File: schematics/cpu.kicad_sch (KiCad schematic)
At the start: 3 parts, among them U3 W65C02SxP

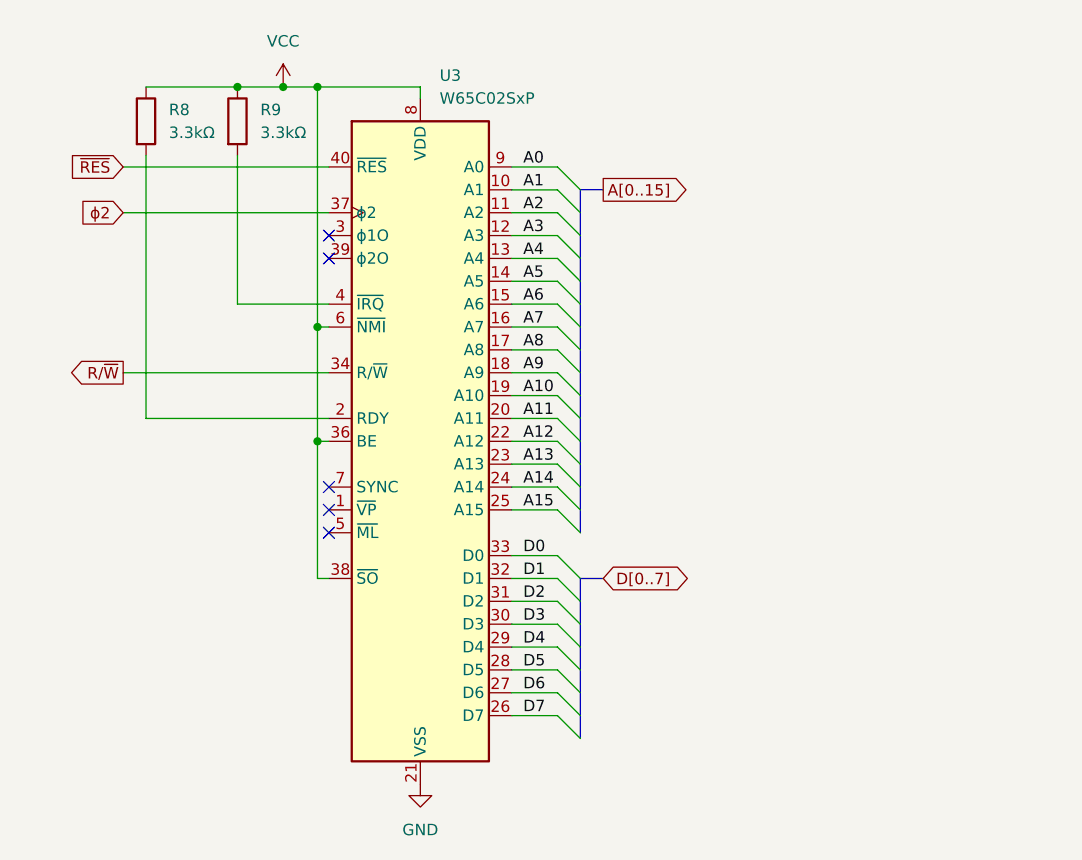
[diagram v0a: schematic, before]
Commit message: Address decoder pld file and no-VIA keyboard schematic and pld file.
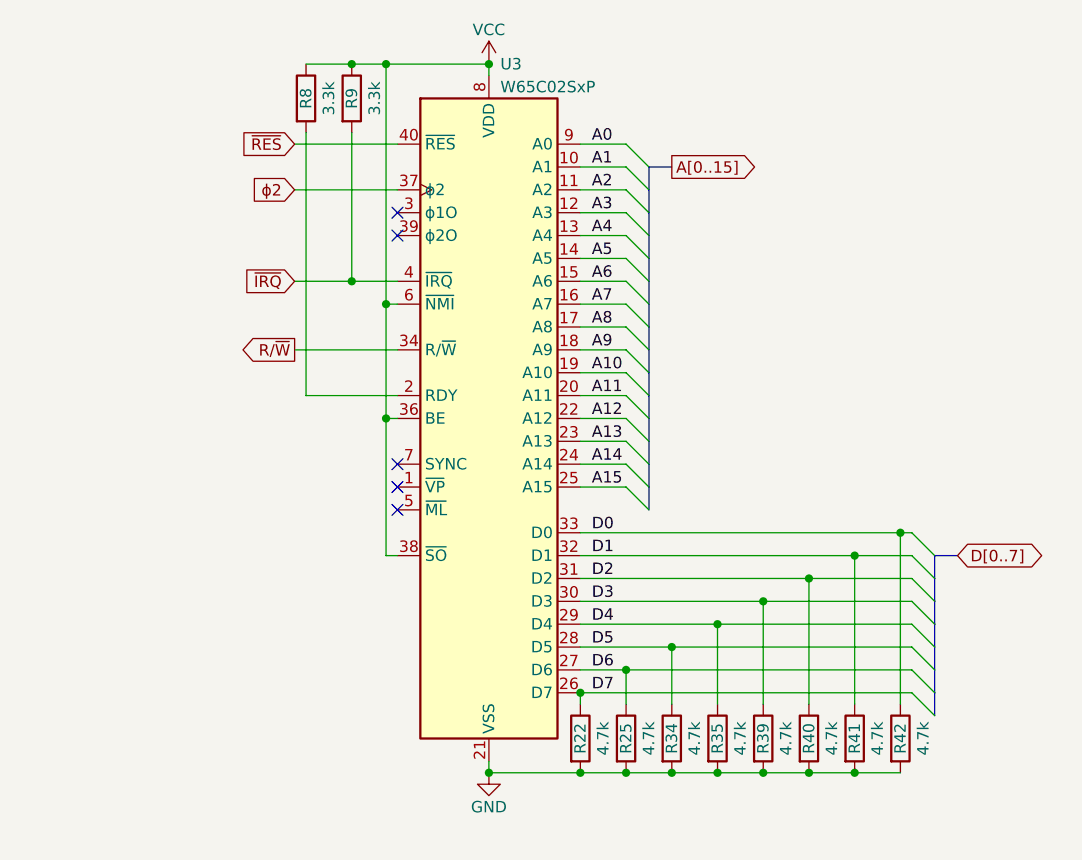
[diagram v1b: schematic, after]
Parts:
- added R22, R25, R34, R35, R39, R40, R41, R42: 4.7k, symbol Device:R
- R8, R9: value 3.3kΩ -> 3.3k
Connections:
- net D0: now also R42.1
- net D1: now also R41.1
- net D2: now also R40.1
- net D3: now also R39.1
- net D4: now also R35.1
- net D5: now also R34.1
- net D6: now also R25.1
- net D7: now also R22.1
- net GND: now also R22.2, R25.2, R34.2, R35.2, R39.2, R40.2, R41.2, R42.2
- net ~{IRQ}: now reaches R9.2, U3.4 (~{IRQ})
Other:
- moved on the sheet: R8, R9, U3

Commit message: PLD files and schematics for address decoder, device selector, keyboard controller, lcd controller, banked memory, and bootloader.
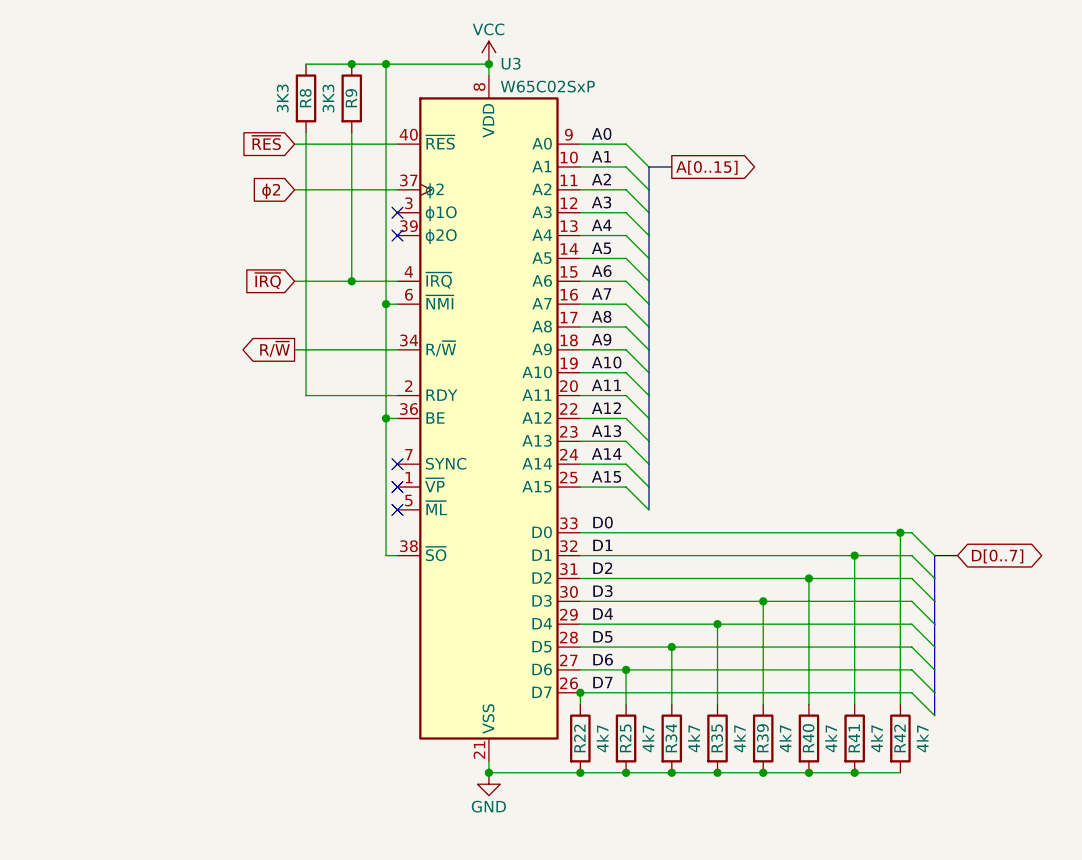
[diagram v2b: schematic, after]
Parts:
- R22, R25, R34, R35, R39, R40, R41, R42: value 4.7k -> 4k7
- R8, R9: value 3.3k -> 3K3
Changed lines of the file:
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@@
 			)
 		)
-		(property "Value" "4.7k"
+		(property "Value" "4k7"
 			(at 177.8 134.62 90)
 			(show_name no)
@@
 			)
 		)
-		(property "Value" "4.7k"
+		(property "Value" "4k7"
 			(at 172.72 134.62 90)
 			(show_name no)
@@
 			)
 		)
-		(property "Value" "4.7k"
+		(property "Value" "4k7"
 			(at 162.56 134.62 90)
 			(show_name no)
@@
 			)
 		)
-		(property "Value" "3.3k"
-			(at 121.92 63.5 90)
+		(property "Value" "3K3"
+			(at 116.84 63.5 90)
 			(show_name no)
 			(do_not_autoplace no)
@@
 			)
 		)
-		(property "Value" "4.7k"
+		(property "Value" "4k7"
 			(at 147.32 134.62 90)
 			(show_name no)
@@
 			)
 		)
-		(property "Value" "3.3k"
-			(at 116.84 63.5 90)
+		(property "Value" "3K3"
+			(at 111.76 63.5 90)
 			(show_name no)
 			(do_not_autoplace no)
@@
 			)
 		)
-		(property "Value" "4.7k"
+		(property "Value" "4k7"
 			(at 152.4 134.62 90)
 			(show_name no)
@@
 			)
 		)
-		(property "Value" "4.7k"
+		(property "Value" "4k7"
 			(at 182.88 134.62 90)
 			(show_name no)
@@
 			)
 		)
-		(property "Value" "4.7k"
+		(property "Value" "4k7"
 			(at 167.64 134.62 90)
 			(show_name no)
@@
 			)
 		)
-		(property "Value" "4.7k"
+		(property "Value" "4k7"
 			(at 157.48 134.62 90)
 			(show_name no)

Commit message: reduced RDY pullup to 1K for speed (still might not be enough)
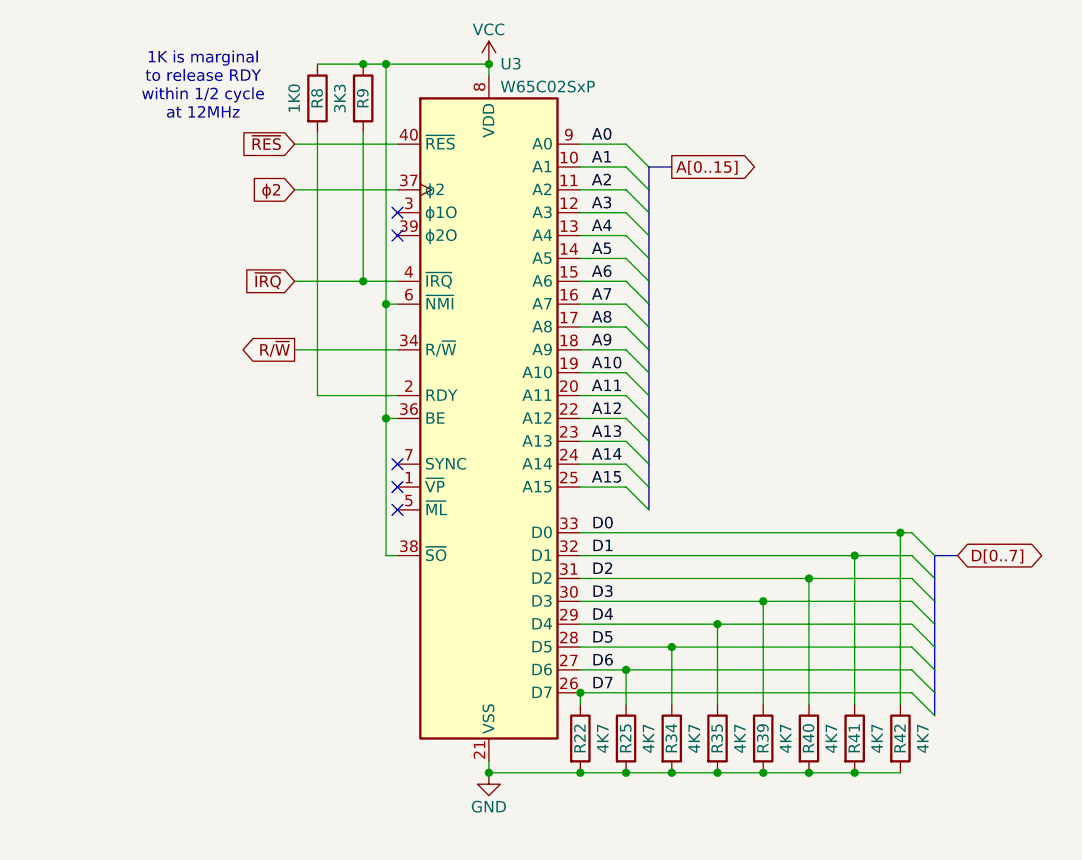
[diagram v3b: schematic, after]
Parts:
- R22, R25, R34, R35, R39, R40, R41, R42: value 4k7 -> 4K7
- R8: value 3K3 -> 1K0
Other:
- note added: "1K is marginal to release RDY within 1/2 cycle at 12MHz"
- moved on the sheet: R8, R9
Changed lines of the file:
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@@
 		(rev "1")
+	)
+	(text "1K is marginal\nto release RDY\nwithin 1/2 cycle\nat 12MHz"
+		(exclude_from_sim no)
+		(at 102.87 62.23 0)
+		(effects
+			(font
+				(size 1.27 1.27)
+			)
+		)
 	)
 	(junction
@@
 	)
 	(junction
+		(at 120.65 59.69)
+		(diameter 0)
+		(color 0 0 0 0)
+	)
+	(junction
 		(at 149.86 127)
 		(diameter 0)
@@
 	)
 	(junction
-		(at 119.38 59.69)
-		(diameter 0)
-		(color 0 0 0 0)
-	)
-	(junction
 		(at 144.78 129.54)
-		(diameter 0)
-		(color 0 0 0 0)
-	)
-	(junction
-		(at 119.38 83.82)
 		(diameter 0)
 		(color 0 0 0 0)
@@
 		(color 0 0 0 0)
 	)
+	(junction
+		(at 120.65 83.82)
+		(diameter 0)
+		(color 0 0 0 0)
+	)
 	(no_connect
 		(at 124.46 76.2)
@@
 	(wire
 		(pts
-			(xy 119.38 67.31) (xy 119.38 83.82)
+			(xy 120.65 67.31) (xy 120.65 83.82)
 		)
 		(stroke
@@
 	(wire
 		(pts
-			(xy 124.46 96.52) (xy 114.3 96.52)
+			(xy 124.46 96.52) (xy 115.57 96.52)
 		)
 		(stroke
@@
 		)
 	)
+	(wire
+		(pts
+			(xy 120.65 83.82) (xy 124.46 83.82)
+		)
+		(stroke
+			(width 0)
+			(type default)
+		)
+	)
 	(bus
 		(pts
@@
 	(wire
 		(pts
-			(xy 113.03 83.82) (xy 119.38 83.82)
+			(xy 113.03 83.82) (xy 120.65 83.82)
 		)
 		(stroke
@@
 	(wire
 		(pts
-			(xy 114.3 67.31) (xy 114.3 96.52)
+			(xy 115.57 67.31) (xy 115.57 96.52)
 		)
 		(stroke
@@
 	(wire
 		(pts
-			(xy 119.38 83.82) (xy 124.46 83.82)
-		)
-		(stroke
-			(width 0)
-			(type default)
-		)
-	)
-	(wire
-		(pts
 			(xy 165.1 138.43) (xy 170.18 138.43)
 		)
@@
 	(wire
 		(pts
+			(xy 120.65 59.69) (xy 134.62 59.69)
+		)
+		(stroke
+			(width 0)
+			(type default)
+		)
+	)
+	(wire
+		(pts
 			(xy 144.78 119.38) (xy 165.1 119.38)
 		)
@@
 	(wire
 		(pts
-			(xy 119.38 59.69) (xy 134.62 59.69)
-		)
-		(stroke
-			(width 0)
-			(type default)
-		)
-	)
-	(wire
-		(pts
 			(xy 160.02 138.43) (xy 165.1 138.43)
 		)
@@
 	(wire
 		(pts
-			(xy 114.3 59.69) (xy 119.38 59.69)
+			(xy 115.57 59.69) (xy 120.65 59.69)
 		)
 		(stroke
@@
 			)
 		)
-		(property "Value" "4k7"
+		(property "Value" "4K7"
 			(at 177.8 134.62 90)
 			(show_name no)
@@
 			)
 		)
-		(property "Value" "4k7"
+		(property "Value" "4K7"
 			(at 172.72 134.62 90)
 			(show_name no)
@@
 			)
 		)
-		(property "Value" "4k7"
+		(property "Value" "4K7"
 			(at 162.56 134.62 90)
 			(show_name no)
@@
 	(symbol
 		(lib_id "Device:R")
-		(at 119.38 63.5 0)
+		(at 120.65 63.5 0)
 		(unit 1)
 		(body_style 1)
@@
 		(dnp no)
 		(property "Reference" "R9"
-			(at 119.38 63.5 90)
+			(at 120.65 63.5 90)
 			(show_name no)
 			(do_not_autoplace no)
@@
 		)
 		(property "Value" "3K3"
-			(at 116.84 63.5 90)
+			(at 118.11 63.5 90)
 			(show_name no)
 			(do_not_autoplace no)
@@
 		)
 		(property "Footprint" ""
-			(at 117.602 63.5 90)
+			(at 118.872 63.5 90)
 			(hide yes)
 			(show_name no)
@@
 		)
 		(property "Datasheet" ""
-			(at 119.38 63.5 0)
+			(at 120.65 63.5 0)
 			(hide yes)
 			(show_name no)
@@
 		)
 		(property "Description" "Resistor"
-			(at 119.38 63.5 0)
+			(at 120.65 63.5 0)
 			(hide yes)
 			(show_name no)
@@
 			)
 		)
-		(property "Value" "4k7"
+		(property "Value" "4K7"
 			(at 147.32 134.62 90)
 			(show_name no)
@@
 	(symbol
 		(lib_id "Device:R")
-		(at 114.3 63.5 0)
+		(at 115.57 63.5 0)
 		(unit 1)
 		(body_style 1)
@@
 		(dnp no)
 		(property "Reference" "R8"
-			(at 114.3 63.5 90)
-			(show_name no)
-			(do_not_autoplace no)
-			(effects
-				(font
-					(size 1.27 1.27)
-				)
-			)
-		)
-		(property "Value" "3K3"
-			(at 111.76 63.5 90)
+			(at 115.57 63.5 90)
+			(show_name no)
+			(do_not_autoplace no)
+			(effects
+				(font
+					(size 1.27 1.27)
+				)
+			)
+		)
+		(property "Value" "1K0"
+			(at 113.03 63.5 90)
 			(show_name no)
 			(do_not_autoplace no)
@@
 		)
 		(property "Footprint" ""
-			(at 112.522 63.5 90)
+			(at 113.792 63.5 90)
 			(hide yes)
 			(show_name no)
@@
 		)
 		(property "Datasheet" ""
-			(at 114.3 63.5 0)
+			(at 115.57 63.5 0)
 			(hide yes)
 			(show_name no)
@@
 		)
 		(property "Description" "Resistor"
-			(at 114.3 63.5 0)
+			(at 115.57 63.5 0)
 			(hide yes)
 			(show_name no)
@@
 			)
 		)
-		(property "Value" "4k7"
+		(property "Value" "4K7"
 			(at 152.4 134.62 90)
 			(show_name no)
@@
 			)
 		)
-		(property "Value" "4k7"
+		(property "Value" "4K7"
 			(at 182.88 134.62 90)
 			(show_name no)
@@
 			)
 		)
-		(property "Value" "4k7"
+		(property "Value" "4K7"
 			(at 167.64 134.62 90)
 			(show_name no)
@@
 			)
 		)
-		(property "Value" "4k7"
+		(property "Value" "4K7"
 			(at 157.48 134.62 90)
 			(show_name no)

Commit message: fixes to bootloader; finished via schematic
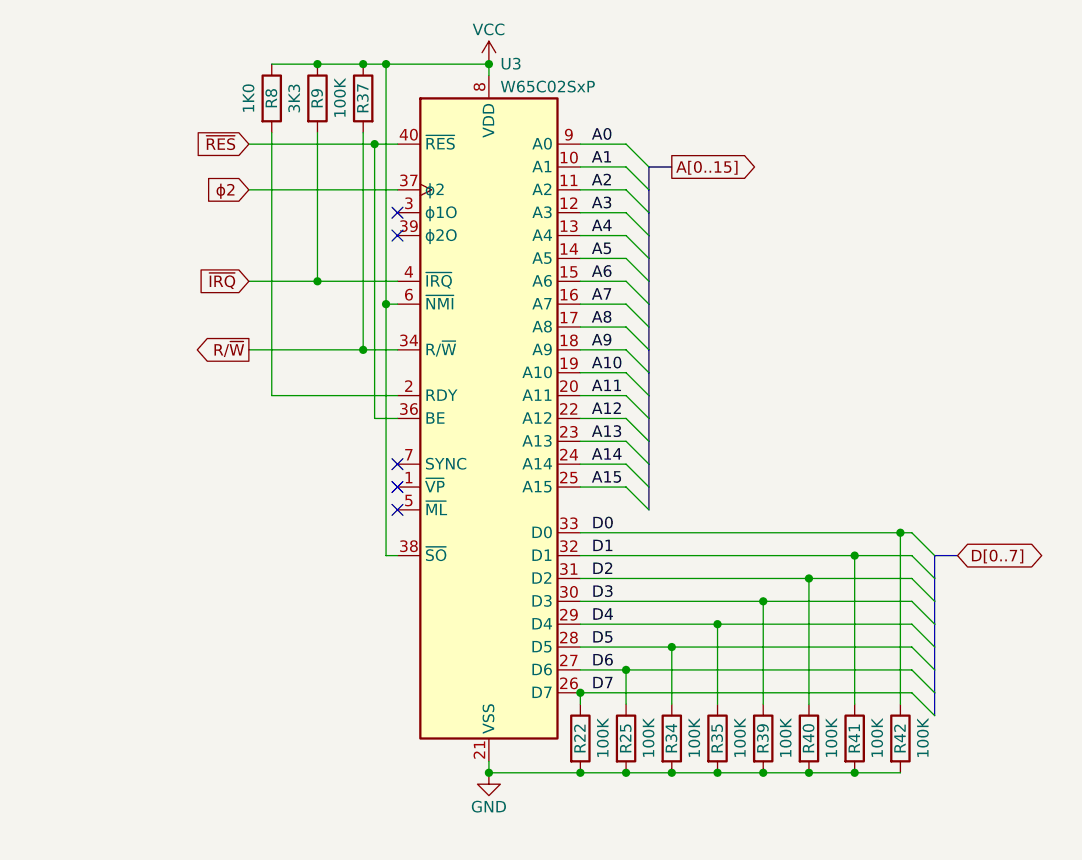
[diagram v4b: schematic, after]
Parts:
- added R37: 100K, symbol Device:R
- R22, R25, R34, R35, R39, R40, R41, R42: value 4K7 -> 100K
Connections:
- net R/~{W}: now also R37.2
- net VCC: now also R37.1; no longer U3.36 (BE)
- net ~{RES}: now also U3.36 (BE)
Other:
- note removed: "1K is marginal to release RDY within 1/2 cycle at 12MHz"
- moved on the sheet: R8, R9

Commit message: updating schematics as I wire the board
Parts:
- R16: renamed from R37; value 100K -> 47K
- R17: renamed from R22; value 100K -> 47K
- R18: renamed from R25; value 100K -> 47K
- R19: renamed from R34; value 100K -> 47K
- R20: renamed from R35; value 100K -> 47K
- R21: renamed from R39; value 100K -> 47K
- R22: renamed from R40; value 100K -> 47K
- R23: renamed from R41; value 100K -> 47K
- R24: renamed from R42; value 100K -> 47K
- renumbered R8 to R14, R9 to R15, U3 to U8
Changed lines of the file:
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@@
 		(in_pos_files yes)
 		(dnp no)
-		(property "Reference" "#PWR010"
+		(property "Reference" "#PWR022"
 			(at 134.62 144.78 0)
 			(hide yes)
@@
 			(project "bv6502_hw"
 				(path "/94c72abe-aaa5-49aa-8ab7-5d3e7cbc10be/fd67868c-cd7d-4cf5-b33e-a271872edf4f"
-					(reference "#PWR010")
+					(reference "#PWR022")
 					(unit 1)
 				)
@@
 		(in_pos_files yes)
 		(dnp no)
-		(property "Reference" "R41"
+		(property "Reference" "R23"
 			(at 175.26 134.62 90)
 			(show_name no)
@@
 			)
 		)
-		(property "Value" "100K"
+		(property "Value" "47K"
 			(at 177.8 134.62 90)
 			(show_name no)
@@
 			(project "bv6502_hw"
 				(path "/94c72abe-aaa5-49aa-8ab7-5d3e7cbc10be/fd67868c-cd7d-4cf5-b33e-a271872edf4f"
-					(reference "R41")
+					(reference "R23")
 					(unit 1)
 				)
@@
 		(in_pos_files yes)
 		(dnp no)
-		(property "Reference" "R40"
+		(property "Reference" "R22"
 			(at 170.18 134.62 90)
 			(show_name no)
@@
 			)
 		)
-		(property "Value" "100K"
+		(property "Value" "47K"
 			(at 172.72 134.62 90)
 			(show_name no)
@@
 			(project "bv6502_hw"
 				(path "/94c72abe-aaa5-49aa-8ab7-5d3e7cbc10be/fd67868c-cd7d-4cf5-b33e-a271872edf4f"
-					(reference "R40")
+					(reference "R22")
 					(unit 1)
 				)
@@
 		(in_pos_files yes)
 		(dnp no)
-		(property "Reference" "R35"
+		(property "Reference" "R20"
 			(at 160.02 134.62 90)
 			(show_name no)
@@
 			)
 		)
-		(property "Value" "100K"
+		(property "Value" "47K"
 			(at 162.56 134.62 90)
 			(show_name no)
@@
 			(project "bv6502_hw"
 				(path "/94c72abe-aaa5-49aa-8ab7-5d3e7cbc10be/fd67868c-cd7d-4cf5-b33e-a271872edf4f"
-					(reference "R35")
+					(reference "R20")
 					(unit 1)
 				)
@@
 		(in_pos_files yes)
 		(dnp no)
-		(property "Reference" "R9"
+		(property "Reference" "R15"
 			(at 115.57 63.5 90)
 			(show_name no)
@@
 			(project "bv6502_hw"
 				(path "/94c72abe-aaa5-49aa-8ab7-5d3e7cbc10be/fd67868c-cd7d-4cf5-b33e-a271872edf4f"
-					(reference "R9")
+					(reference "R15")
 					(unit 1)
 				)
@@
 		(in_pos_files yes)
 		(dnp no)
-		(property "Reference" "R37"
+		(property "Reference" "R16"
 			(at 120.65 63.5 90)
 			(show_name no)
@@
 			)
 		)
-		(property "Value" "100K"
+		(property "Value" "47K"
 			(at 118.11 63.5 90)
 			(show_name no)
@@
 			(project "bv6502_hw"
 				(path "/94c72abe-aaa5-49aa-8ab7-5d3e7cbc10be/fd67868c-cd7d-4cf5-b33e-a271872edf4f"
-					(reference "R37")
+					(reference "R16")
 					(unit 1)
 				)
@@
 		(in_pos_files yes)
 		(dnp no)
-		(property "Reference" "R22"
+		(property "Reference" "R17"
 			(at 144.78 134.62 90)
 			(show_name no)
@@
 			)
 		)
-		(property "Value" "100K"
+		(property "Value" "47K"
 			(at 147.32 134.62 90)
 			(show_name no)
@@
 			(project "bv6502_hw"
 				(path "/94c72abe-aaa5-49aa-8ab7-5d3e7cbc10be/fd67868c-cd7d-4cf5-b33e-a271872edf4f"
-					(reference "R22")
+					(reference "R17")
 					(unit 1)
 				)
@@
 		(in_pos_files yes)
 		(dnp no)
-		(property "Reference" "R8"
+		(property "Reference" "R14"
 			(at 110.49 63.5 90)
 			(show_name no)
@@
 			(project "bv6502_hw"
 				(path "/94c72abe-aaa5-49aa-8ab7-5d3e7cbc10be/fd67868c-cd7d-4cf5-b33e-a271872edf4f"
-					(reference "R8")
+					(reference "R14")
 					(unit 1)
 				)
@@
 		(in_pos_files yes)
 		(dnp no)
-		(property "Reference" "R25"
+		(property "Reference" "R18"
 			(at 149.86 134.62 90)
 			(show_name no)
@@
 			)
 		)
-		(property "Value" "100K"
+		(property "Value" "47K"
 			(at 152.4 134.62 90)
 			(show_name no)
@@
 			(project "bv6502_hw"
 				(path "/94c72abe-aaa5-49aa-8ab7-5d3e7cbc10be/fd67868c-cd7d-4cf5-b33e-a271872edf4f"
-					(reference "R25")
+					(reference "R18")
 					(unit 1)
 				)
@@
 		(in_pos_files yes)
 		(dnp no)
-		(property "Reference" "R42"
+		(property "Reference" "R24"
 			(at 180.34 134.62 90)
 			(show_name no)
@@
 			)
 		)
-		(property "Value" "100K"
+		(property "Value" "47K"
 			(at 182.88 134.62 90)
 			(show_name no)
@@
 			(project "bv6502_hw"
 				(path "/94c72abe-aaa5-49aa-8ab7-5d3e7cbc10be/fd67868c-cd7d-4cf5-b33e-a271872edf4f"
-					(reference "R42")
+					(reference "R24")
 					(unit 1)
 				)
@@
 		(in_pos_files yes)
 		(dnp no)
-		(property "Reference" "R39"
+		(property "Reference" "R21"
 			(at 165.1 134.62 90)
 			(show_name no)
@@
 			)
 		)
-		(property "Value" "100K"
+		(property "Value" "47K"
 			(at 167.64 134.62 90)
 			(show_name no)
@@
 			(project "bv6502_hw"
 				(path "/94c72abe-aaa5-49aa-8ab7-5d3e7cbc10be/fd67868c-cd7d-4cf5-b33e-a271872edf4f"
-					(reference "R39")
+					(reference "R21")
 					(unit 1)
 				)
@@
 		(in_pos_files yes)
 		(dnp no)
-		(property "Reference" "#PWR09"
+		(property "Reference" "#PWR021"
 			(at 134.62 63.5 0)
 			(hide yes)
@@
 			(project "bv6502_hw"
 				(path "/94c72abe-aaa5-49aa-8ab7-5d3e7cbc10be/fd67868c-cd7d-4cf5-b33e-a271872edf4f"
-					(reference "#PWR09")
+					(reference "#PWR021")
 					(unit 1)
 				)
@@
 		(in_pos_files yes)
 		(dnp no)
-		(property "Reference" "R34"
+		(property "Reference" "R19"
 			(at 154.94 134.62 90)
 			(show_name no)
@@
 			)
 		)
-		(property "Value" "100K"
+		(property "Value" "47K"
 			(at 157.48 134.62 90)
 			(show_name no)
@@
 			(project "bv6502_hw"
 				(path "/94c72abe-aaa5-49aa-8ab7-5d3e7cbc10be/fd67868c-cd7d-4cf5-b33e-a271872edf4f"
-					(reference "R34")
+					(reference "R19")
 					(unit 1)
 				)
@@
 		(in_pos_files yes)
 		(dnp no)
-		(property "Reference" "U3"
+		(property "Reference" "U8"
 			(at 135.89 59.69 0)
 			(show_name no)
@@
 			(project "bv6502_hw"
 				(path "/94c72abe-aaa5-49aa-8ab7-5d3e7cbc10be/fd67868c-cd7d-4cf5-b33e-a271872edf4f"
-					(reference "U3")
-					(unit 1)
-				)
+					(reference "U8")
+					(unit 1)
+				)
